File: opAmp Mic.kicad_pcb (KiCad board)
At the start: 2 copper layers, 19 x 80.5 mm, 23 parts, among them J1 XLR3

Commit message: made the capsule ground sit on the chassis rather than the virtual ground, which solves some of the issues I had with the initial pcb run
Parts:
- MK1: renamed from TS 2555; value electret -> Microphone
- R10, R9: value 47R -> 47
- R6: value 200R -> 200
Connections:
- MK1 pad 1: GND -> Earth
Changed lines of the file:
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@@
     (at 120.9802 64.3636 180)
     (descr http://www.molex.com/pdm_docs/sd/022232031_sd.pdf)
-    (fp_text reference "TS 2555" (at 1.1684 2.0574) (layer F.SilkS)
-      (effects (font (size 1 1) (thickness 0.15)))
-    )
-    (fp_text value electret (at 1.1684 -2.1336) (layer F.SilkS)
+    (fp_text reference MK1 (at 1.1684 2.0574) (layer F.SilkS)
+      (effects (font (size 1 1) (thickness 0.15)))
+    )
+    (fp_text value Microphone (at 1.1684 -2.1336) (layer F.SilkS)
       (effects (font (size 1 1) (thickness 0.15)))
     )
@@
     (fp_line (start -1.2 -3.17) (end 3.73 -3.17) (layer F.Fab) (width 0.1))
     (pad 1 thru_hole circle (at 0 0 180) (size 2.02 2.02) (drill 1.02) (layers *.Cu *.Mask)
-      (net 3 GND))
+      (net 2 Earth))
     (pad 2 thru_hole circle (at 2.54 0 180) (size 2.02 2.02) (drill 1.02) (layers *.Cu *.Mask)
       (net 11 "Net-(MK1-Pad2)"))
@@
       (effects (font (size 1 1) (thickness 0.15)))
     )
-    (fp_text value 200R (at -1.905 -1.0414 180) (layer F.SilkS)
+    (fp_text value 200 (at -1.905 -1.0414 180) (layer F.SilkS)
       (effects (font (size 1 1) (thickness 0.15)))
     )
@@
       (effects (font (size 1 1) (thickness 0.15)))
     )
-    (fp_text value 47R (at 2.54 1.8288 90) (layer F.SilkS)
+    (fp_text value 47 (at 2.54 1.8288 90) (layer F.SilkS)
       (effects (font (size 1 1) (thickness 0.15)))
     )
@@
       (effects (font (size 1 1) (thickness 0.15)))
     )
-    (fp_text value 47R (at 2.54 1.8542 90) (layer F.SilkS)
-      (effects (font (size 1 1) (thickness 0.15)))
-    )
+    (fp_text value 47 (at 2.54 1.8542 90) (layer F.SilkS)
+      (effects (font (size 1 1) (thickness 0.15)))
+    )

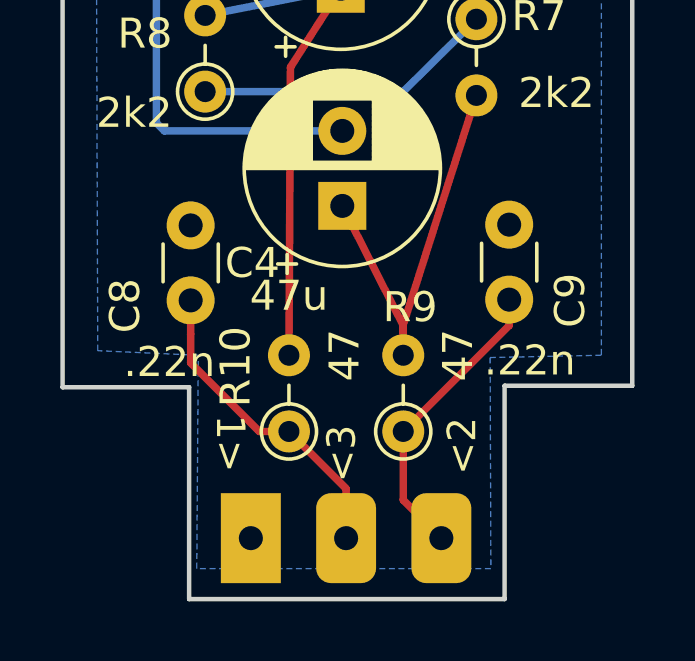
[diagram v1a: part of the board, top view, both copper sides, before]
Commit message: changed a few screenprints, and modified the xlr connector 1st commit using different command line on different computer, lets see how it works
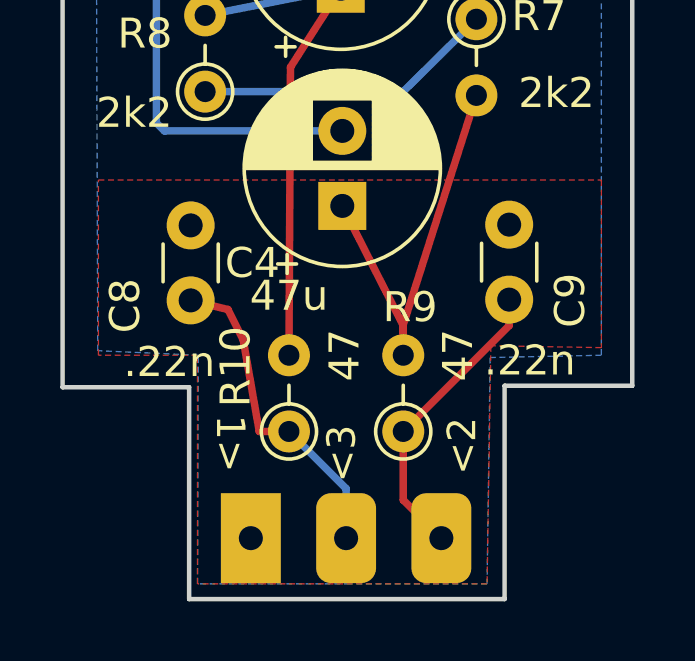
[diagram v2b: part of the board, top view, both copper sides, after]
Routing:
- added copper zone on F.Cu, net Earth
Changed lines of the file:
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@@
-(kicad_pcb (version 20171130) (host pcbnew "(5.1.5)-3")
+(kicad_pcb (version 20171130) (host pcbnew "(5.1.2-1)-1")
   (general
     (thickness 1.6)
@@
     (mod_text_size 1 1)
     (mod_text_width 0.15)
-    (pad_size 2.02 2.02)
-    (pad_drill 1.02)
+    (pad_size 1.99898 3)
+    (pad_drill 0.8001)
     (pad_to_mask_clearance 0.051)
     (solder_mask_min_width 0.25)
@@
       (effects (font (size 0.9652 0.9652) (thickness 0.07112)) (justify right top))
     )
-    (pad 2 thru_hole roundrect (at 3.175 0) (size 1.99898 3) (drill 0.8001) (layers *.Cu *.Mask) (roundrect_rratio 0.25)
+    (pad 2 thru_hole roundrect (at 3.175 0) (size 1.99898 3) (drill 0.8001) (layers *.Mask F.Cu) (roundrect_rratio 0.25)
       (net 10 "Net-(C9-Pad1)"))
-    (pad 3 thru_hole roundrect (at 0 0) (size 1.99898 3) (drill 0.8001) (layers *.Cu *.Mask) (roundrect_rratio 0.25)
+    (pad 3 thru_hole roundrect (at 0 0) (size 1.99898 3) (drill 0.8001) (layers *.Mask B.Cu) (roundrect_rratio 0.25)
       (net 9 "Net-(C8-Pad1)"))
-    (pad 1 thru_hole rect (at -3.175 0) (size 1.99898 3) (drill 0.8001) (layers *.Cu *.Mask)
+    (pad 1 thru_hole rect (at -3.175 0) (size 1.99898 3) (drill 0.8001) (layers *.Mask F.Cu)
       (net 2 Earth))
   )
@@
   (segment (start 120.904 123.5456) (end 123.3424 121.1326) (width 0.25) (layer B.Cu) (net 8))
   (segment (start 114.3 123.5456) (end 120.904 123.5456) (width 0.25) (layer B.Cu) (net 8))
-  (segment (start 118.999 136.779) (end 117.094 134.874) (width 0.25) (layer F.Cu) (net 9))
-  (segment (start 118.999 138.43) (end 118.999 136.779) (width 0.25) (layer F.Cu) (net 9))
-  (segment (start 113.8174 132.587349) (end 113.8174 131.63657) (width 0.25) (layer F.Cu) (net 9))
-  (segment (start 116.104051 134.874) (end 113.8174 132.587349) (width 0.25) (layer F.Cu) (net 9))
-  (segment (start 113.8174 131.63657) (end 113.8174 130.5052) (width 0.25) (layer F.Cu) (net 9))
+  (segment (start 118.999 136.779) (end 117.094 134.874) (width 0.25) (layer B.Cu) (net 9))
+  (segment (start 118.999 138.43) (end 118.999 136.779) (width 0.25) (layer B.Cu) (net 9))
+  (segment (start 115.062 130.81) (end 113.8174 130.5052) (width 0.25) (layer F.Cu) (net 9))
+  (segment (start 115.57 131.826) (end 115.062 130.81) (width 0.25) (layer F.Cu) (net 9))
+  (segment (start 116.104051 134.874) (end 115.57 131.826) (width 0.25) (layer F.Cu) (net 9))
   (segment (start 117.094 134.874) (end 116.104051 134.874) (width 0.25) (layer F.Cu) (net 9))
   (segment (start 120.904 137.16) (end 120.904 134.874) (width 0.25) (layer F.Cu) (net 10))
@@
     (polygon
       (pts
-        (xy 127.508 132.334) (xy 123.7996 132.4102) (xy 123.825 139.446) (xy 119.126 139.446) (xy 114.0206 139.446)
+        (xy 127.508 132.334) (xy 123.7996 132.4102) (xy 123.698 139.954) (xy 119.126 139.954) (xy 114.046 139.954)
         (xy 114.0714 132.334) (xy 110.72026 132.181429) (xy 110.49 61.722) (xy 127.508 61.722)
       )
     )
+  )
+  (zone (net 2) (net_name Earth) (layer F.Cu) (hatch edge 0.508)
+    (connect_pads (clearance 0.508))
+    (min_thickness 0.254)
+    (fill yes (arc_segments 32) (thermal_gap 0.508) (thermal_bridge_width 0.508))
+    (polygon
+      (pts
+        (xy 110.744 126.492) (xy 127.508 126.492) (xy 127.508 132.08) (xy 123.825 132.0165) (xy 123.698 139.954)
+        (xy 114.046 139.954) (xy 114.046 132.334) (xy 110.744 132.334)
+      )
+    )
